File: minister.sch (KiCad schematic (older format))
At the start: 108 parts

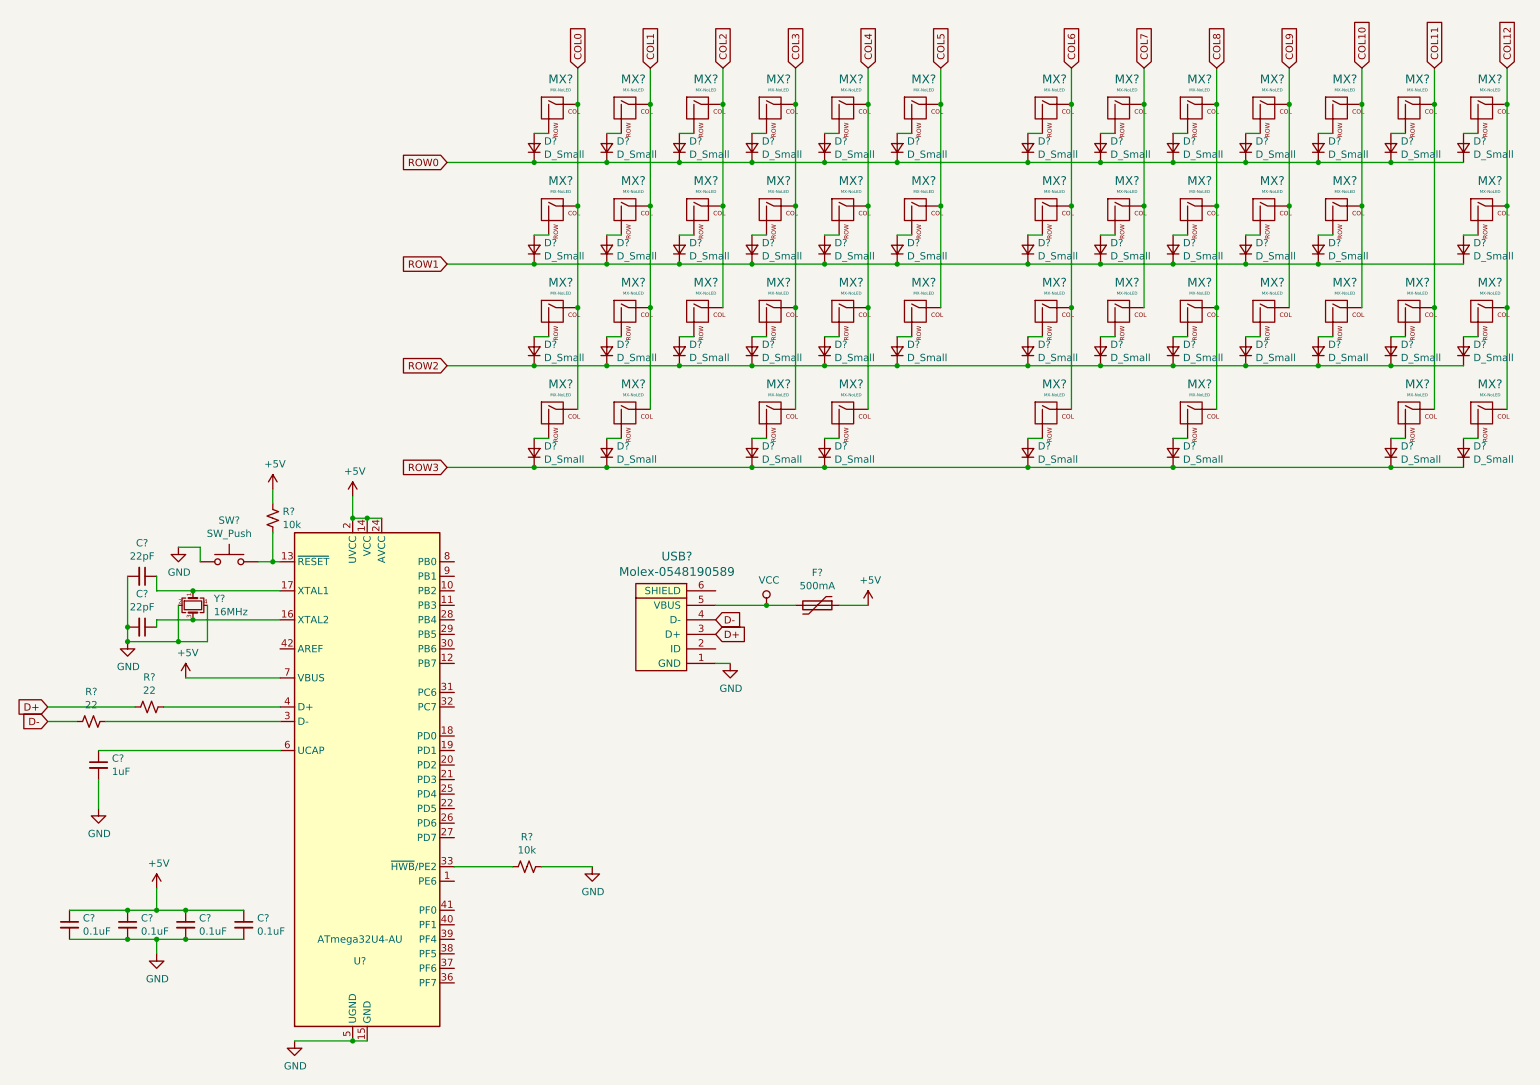
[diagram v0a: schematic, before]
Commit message: Assign Footprints
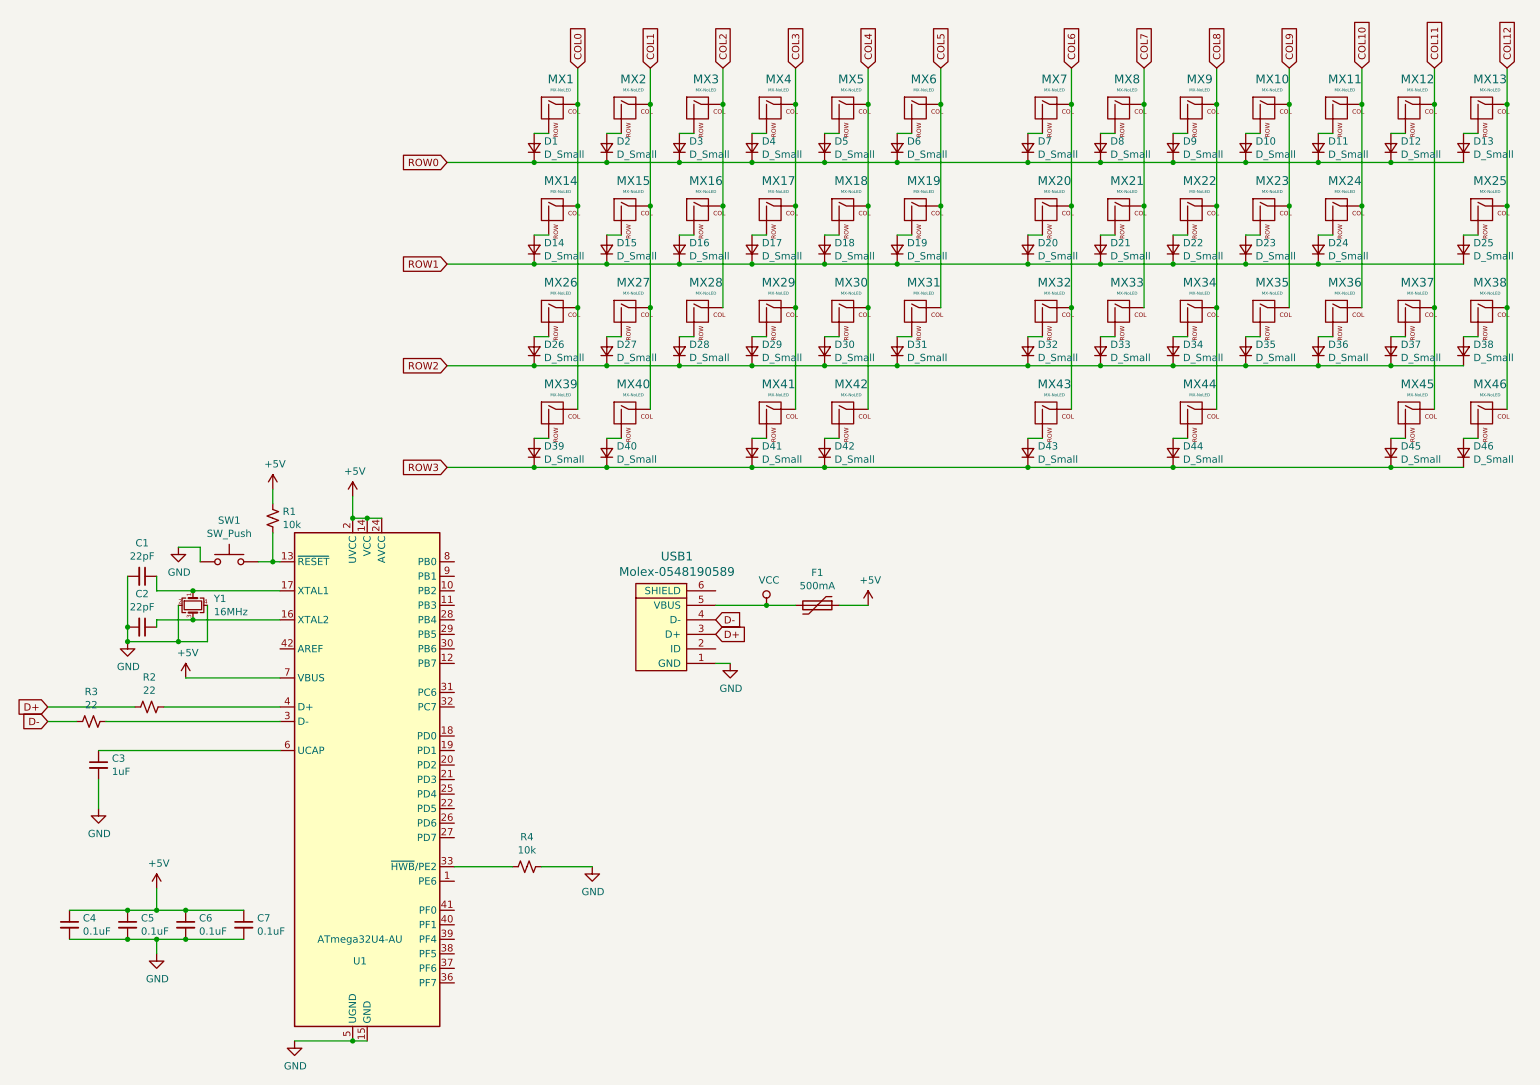
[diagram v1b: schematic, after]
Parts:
- C1, C2, C3, C4, C5, C6, C7: renamed from C?; footprint (none) -> Capacitor_SMD:C_0805_2012Metric
- D1, D10, D11, D12, D13, D14, D15, D16, D17, D18, D19, D2, D20, D21, D22, D23, D24, D25, D26, D27, D28, D29, D3, D30, D31, D32, D33, D34, D35, D36, D37, D38, D39, D4, D40, D41, D42, D43, D44, D45, D46, D5, D6, D7, D8, D9: renamed from D?; footprint (none) -> Diode_SMD:D_SOD-123
- F1: renamed from F?; footprint (none) -> Fuse:Fuse_1206_3216Metric
- MX1, MX10, MX11, MX12, MX13, MX14, MX15, MX16, MX17, MX18, MX19, MX2, MX20, MX21, MX22, MX23, MX24, MX25, MX26, MX27, MX28, MX29, MX3, MX30, MX31, MX32, MX33, MX34, MX35, MX36, MX37, MX38, MX39, MX4, MX40, MX41, MX42, MX43, MX44, MX45, MX46, MX5, MX6, MX7, MX8, MX9: renamed from MX?; footprint (none) -> MX_Only:MXOnly-1U
- R1, R2, R3, R4: renamed from R?; footprint (none) -> Resistor_SMD:R_0805_2012Metric
- SW1: renamed from SW?; footprint (none) -> random-keyboard-parts:SKQG-1155865
- USB1: renamed from USB?; footprint (none) -> random-keyboard-parts:Molex-0548190589
- Y1: renamed from Y?; footprint (none) -> Crystal:Crystal_SMD_3225-4Pin_3.2x2.5mm
- gave numbers to parts that had none: 1

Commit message: update footprints
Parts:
- MX1, MX10, MX11, MX12, MX13, MX15, MX16, MX17, MX18, MX19, MX2, MX20, MX21, MX22, MX23, MX24, MX27, MX28, MX29, MX3, MX30, MX31, MX32, MX33, MX34, MX35, MX36, MX37, MX4, MX5, MX6, MX7, MX8, MX9: footprint MX_Only:MXOnly-1U -> MX_Only:MXOnly-1U-Hotswap
- MX14, MX38, MX39, MX40, MX41, MX44, MX45, MX46: footprint MX_Only:MXOnly-1U -> MX_Only:MXOnly-1.25U-Hotswap
- MX25, MX26: footprint MX_Only:MXOnly-1U -> MX_Only:MXOnly-1.75U-Hotswap
- MX42: footprint MX_Only:MXOnly-1U -> MX_Only:MXOnly-2U-Hotswap
- MX43: footprint MX_Only:MXOnly-1U -> MX_Only:MXOnly-2.25U-Hotswap

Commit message: rearrange components
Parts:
- C7: value 0.1uF -> 10uF
- MX42: footprint MX_Only:MXOnly-2U-Hotswap -> MX_Only:MXOnly-2U-Hotswap-ReversedStabilizers
- MX43: footprint MX_Only:MXOnly-2.25U-Hotswap -> MX_Only:MXOnly-2.25U-Hotswap-ReversedStabilizers
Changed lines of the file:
@@
 P 2100 6650
 F 0 "C7" H 2192 6696 50  0000 L CNN
-F 1 "0.1uF" H 2192 6605 50  0000 L CNN
+F 1 "10uF" H 2192 6605 50  0000 L CNN
 F 2 "Capacitor_SMD:C_0805_2012Metric" H 2100 6650 50  0001 C CNN
 F 3 "~" H 2100 6650 50  0001 C CNN
@@
 F 0 "MX43" H 7683 3373 60  0000 C CNN
 F 1 "MX-NoLED" H 7683 3299 20  0000 C CNN
-F 2 "MX_Only:MXOnly-2.25U-Hotswap" H 7025 3125 60  0001 C CNN
+F 2 "MX_Only:MXOnly-2.25U-Hotswap-ReversedStabilizers" H 7025 3125 60  0001 C CNN
 F 3 "" H 7025 3125 60  0001 C CNN
 	1    7650 3150
@@
 F 0 "MX42" H 6283 3373 60  0000 C CNN
 F 1 "MX-NoLED" H 6283 3299 20  0000 C CNN
-F 2 "MX_Only:MXOnly-2U-Hotswap" H 5625 3125 60  0001 C CNN
+F 2 "MX_Only:MXOnly-2U-Hotswap-ReversedStabilizers" H 5625 3125 60  0001 C CNN
 F 3 "" H 5625 3125 60  0001 C CNN
 	1    6250 3150

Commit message: more routing
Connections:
- net COL0: now also U1.41 (PF0)
- net COL1: now also U1.40 (PF1)
- net COL10: now also U1.20 (PD2)
- net COL11: now also U1.19 (PD1)
- net COL12: now also U1.18 (PD0)
- net COL2: now also U1.39 (PF4)
- net COL3: now also U1.38 (PF5)
- net COL4: now also U1.37 (PF6)
- net COL5: now also U1.36 (PF7)
- net COL6: now also U1.26 (PD6)
- net COL7: now also U1.25 (PD4)
- net COL8: now also U1.22 (PD5)
- net COL9: now also U1.21 (PD3)
- net ROW0: now also U1.1 (PE6)
- net ROW1: now also U1.32 (PC7)
- net ROW2: now also U1.29 (PB5)
- net ROW3: now also U1.28 (PB4)
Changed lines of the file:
@@
 EESchema Schematic File Version 4
+LIBS:minister-cache
 EELAYER 30 0
 EELAYER END
@@
 Text GLabel 10800 750  1    50   Input ~ 0
 COL12
+Text GLabel 3550 6350 2    50   Input ~ 0
+ROW0
+Text GLabel 3550 5150 2    50   Input ~ 0
+ROW1
+Text GLabel 3550 4650 2    50   Input ~ 0
+ROW2
+Text GLabel 3550 4550 2    50   Input ~ 0
+ROW3
+Text GLabel 3550 6550 2    50   Input ~ 0
+COL0
+Text GLabel 3550 6650 2    50   Input ~ 0
+COL1
+Text GLabel 3550 6750 2    50   Input ~ 0
+COL2
+Text GLabel 3550 6850 2    50   Input ~ 0
+COL3
+Text GLabel 3550 6950 2    50   Input ~ 0
+COL4
+Text GLabel 3550 7050 2    50   Input ~ 0
+COL5
+Text GLabel 3550 5950 2    50   Input ~ 0
+COL6
+Text GLabel 3550 5750 2    50   Input ~ 0
+COL7
+Text GLabel 3550 5850 2    50   Input ~ 0
+COL8
+Text GLabel 3550 5650 2    50   Input ~ 0
+COL9
+Text GLabel 3550 5550 2    50   Input ~ 0
+COL10
+Text GLabel 3550 5450 2    50   Input ~ 0
+COL11
+Text GLabel 3550 5350 2    50   Input ~ 0
+COL12
 $EndSCHEMATC

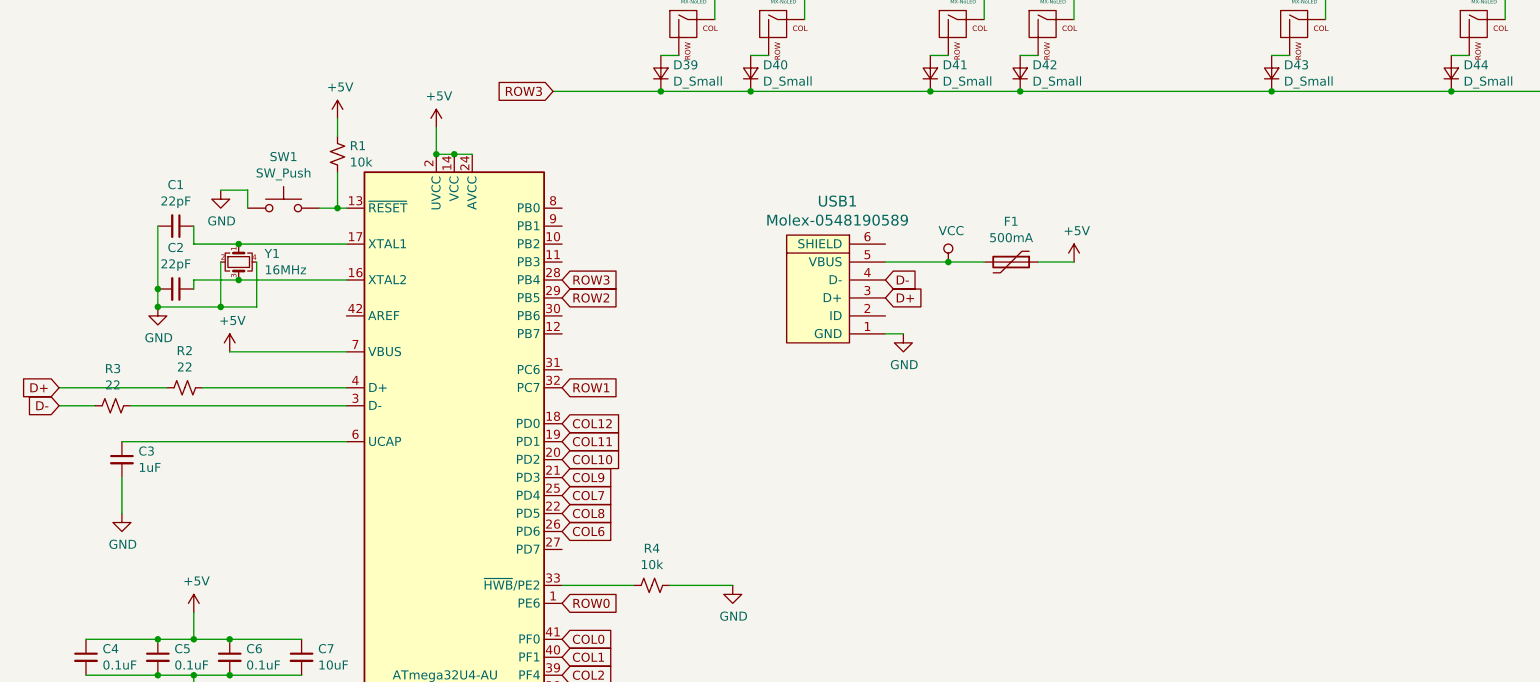
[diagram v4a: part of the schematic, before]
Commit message: replace usb and generate output files
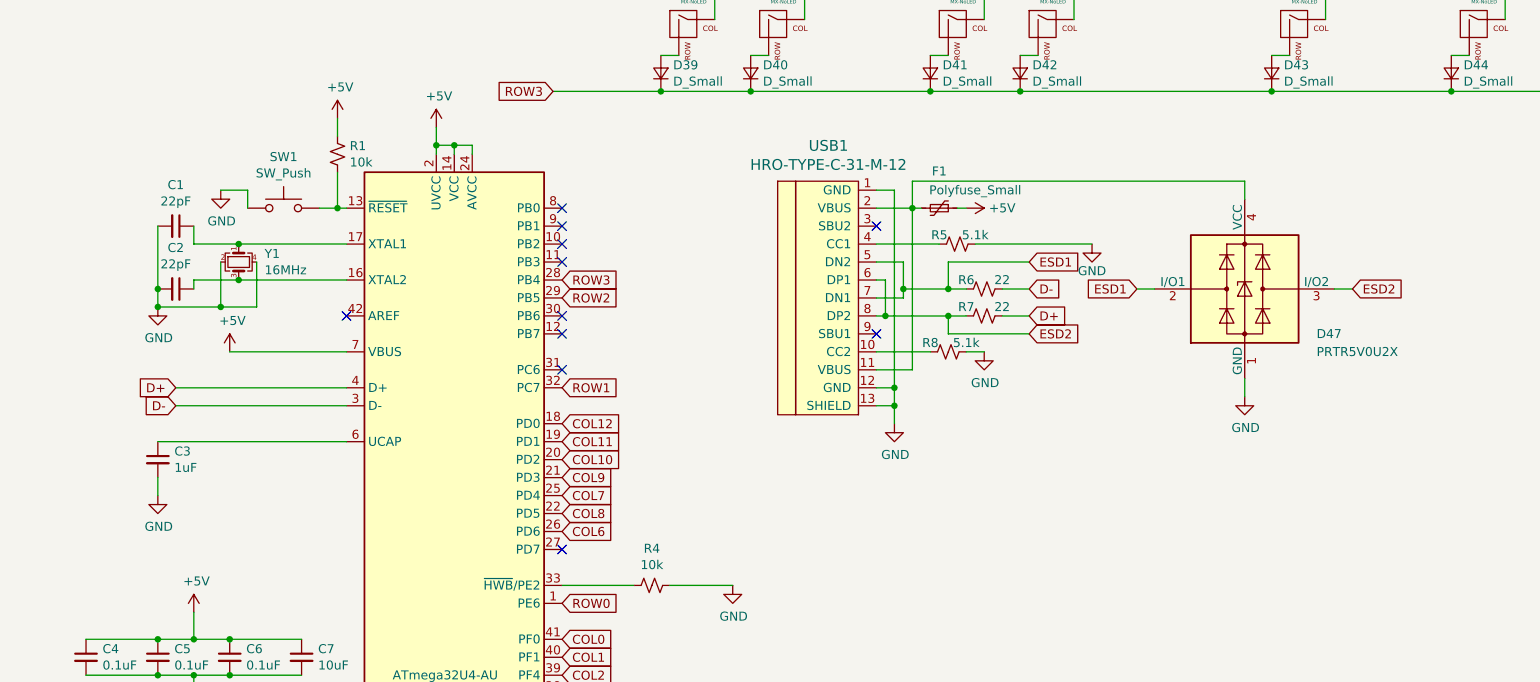
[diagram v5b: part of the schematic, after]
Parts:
- removed F1: 500mA, Fuse:Fuse_1206_3216Metric, symbol Device:Polyfuse
- removed R2, R3: 22, Resistor_SMD:R_0805_2012Metric, symbol Device:R_Small_US
- removed USB1: Molex-0548190589, random-keyboard-parts:Molex-0548190589, symbol random-keyboard-parts:Molex-0548190589
- added D47: PRTR5V0U2X, Package_TO_SOT_SMD:SOT-143_Handsoldering, symbol Power_Protection:PRTR5V0U2X
- added F1: Polyfuse_Small, Fuse:Fuse_1206_3216Metric, symbol Device:Polyfuse_Small
- added R5, R8: 5.1k, Resistor_SMD:R_0805_2012Metric, symbol Device:R_Small_US
- added R6, R7: 22, Resistor_SMD:R_0805_2012Metric, symbol Device:R_Small_US
- added USB1: HRO-TYPE-C-31-M-12, Connector_USB:USB_C_Receptacle_HRO_TYPE-C-31-M-12, symbol Type-C:HRO-TYPE-C-31-M-12
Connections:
- net +5V: now also F1.1
- net D+: now also U1.4 (D+), R7.1
- net D-: now also U1.3 (D-), R6.1
- net GND: now also D47.1 (GND), R5.1, R8.1, USB1.1 (GND), USB1.12 (GND), USB1.13 (SHIELD)
- new net: R8.2, USB1.10 (CC2)
- new net: D47.4 (VCC), F1.2, USB1.11 (VBUS), USB1.2 (VBUS)
- new net: R5.2, USB1.4 (CC1)
- new net ESD1: D47.2 (I/O1), R6.2, USB1.5 (DN2), USB1.7 (DN1)
- new net ESD2: D47.3 (I/O2), R7.2, USB1.6 (DP1), USB1.8 (DP2)
- no-connect marks 0 -> 11
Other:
- moved on the sheet: C3

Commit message: not sure
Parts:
- USB1: footprint Connector_USB:USB_C_Receptacle_HRO_TYPE-C-31-M-12 -> Type-C:HRO-TYPE-C-31-M-12-HandSoldering
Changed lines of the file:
@@
 U 1 1 5E9D7171
 P 5200 4600
-F 0 "USB1" H 5033 5397 60  0000 C CNN
-F 1 "HRO-TYPE-C-31-M-12" H 5033 5291 60  0000 C CNN
-F 2 "Connector_USB:USB_C_Receptacle_HRO_TYPE-C-31-M-12" H 5200 4600 60  0001 C CNN
+F 0 "USB1" H 4850 5250 60  0000 C CNN
+F 1 "HRO-TYPE-C-31-M-12" H 5300 5350 60  0000 C CNN
+F 2 "Type-C:HRO-TYPE-C-31-M-12-HandSoldering" H 5200 4600 60  0001 C CNN
 F 3 "" H 5200 4600 60  0001 C CNN
 	1    5200 4600

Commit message: add isp
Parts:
- added J1: AVR-ISP-6, Connector_IDC:IDC-Header_2x03_P2.54mm_Vertical, symbol Connector:AVR-ISP-6
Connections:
- net +5V: now also J1.2 (VCC)
- net GND: now also J1.6 (GND)
- net MOSI: now reaches U1.10 (PB2)
- net MOSI: now also J1.4 (MOSI)
- net MISO: now reaches U1.11 (PB3)
- net MISO: now also J1.1 (MISO)
- net RST: now reaches R1.2, SW1.2, U1.13 (~RESET)
- net RST: now also J1.5 (~RST)
- net SCK: now reaches U1.9 (PB1)
- net SCK: now also J1.3 (SCK)
- no-connect marks 11 -> 8
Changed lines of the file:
@@
 Wire Wire Line
 	5500 4000 5500 4150
-Wire Wire Line
-	7950 4600 7850 4600
-Text GLabel 7950 4600 2    50   Input ~ 0
+Text GLabel 7850 4600 2    50   Input ~ 0
 ESD2
-Text GLabel 6750 4600 0    50   Input ~ 0
+Text GLabel 6850 4600 0    50   Input ~ 0
 ESD1
-Wire Wire Line
-	6750 4600 6850 4600
 $Comp
 L power:GND #PWR0115
@@
 NoConn ~ 3550 4850
 NoConn ~ 3550 4750
-NoConn ~ 3550 4450
-NoConn ~ 3550 4350
-NoConn ~ 3550 4250
 NoConn ~ 3550 4150
 NoConn ~ 3550 5050
@@
 	1    0    0    -1
 $EndComp
+$Comp
+L Connector:AVR-ISP-6 J1
+U 1 1 5EAF29DC
+P 5750 6300
+F 0 "J1" H 5471 6396 50  0000 R CNN
+F 1 "AVR-ISP-6" H 5471 6305 50  0000 R CNN
+F 2 "Connector_IDC:IDC-Header_2x03_P2.54mm_Vertical" V 5500 6350 50  0001 C CNN
+F 3 " ~" H 4475 5750 50  0001 C CNN
+	1    5750 6300
+	1    0    0    -1
+$EndComp
+Text GLabel 6150 6200 2    50   Input ~ 0
+MOSI
+Text GLabel 6150 6100 2    50   Input ~ 0
+MISO
+Text GLabel 6150 6300 2    50   Input ~ 0
+SCK
+Text GLabel 6150 6400 2    50   Input ~ 0
+RST
+$Comp
+L power:+5V #PWR0116
+U 1 1 5EB30166
+P 5650 5700
+F 0 "#PWR0116" H 5650 5550 50  0001 C CNN
+F 1 "+5V" H 5665 5873 50  0000 C CNN
+F 2 "" H 5650 5700 50  0001 C CNN
+F 3 "" H 5650 5700 50  0001 C CNN
+	1    5650 5700
+	1    0    0    -1
+$EndComp
+$Comp
+L power:GND #PWR0117
+U 1 1 5EB30E0E
+P 5650 6800
+F 0 "#PWR0117" H 5650 6550 50  0001 C CNN
+F 1 "GND" H 5655 6627 50  0000 C CNN
+F 2 "" H 5650 6800 50  0001 C CNN
+F 3 "" H 5650 6800 50  0001 C CNN
+	1    5650 6800
+	1    0    0    -1
+$EndComp
+Wire Wire Line
+	5650 6700 5650 6800
+Wire Wire Line
+	5650 5800 5650 5700
+Text GLabel 3550 4450 2    50   Input ~ 0
+MISO
+Text GLabel 3550 4350 2    50   Input ~ 0
+MOSI
+Text GLabel 3550 4250 2    50   Input ~ 0
+SCK
+Text GLabel 2250 4250 0    50   Input ~ 0
+RST
+Wire Wire Line
+	2250 4250 2300 4250
+Wire Wire Line
+	2300 4250 2300 4150
 $EndSCHEMATC

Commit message: clean up and touch up pcb
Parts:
- C1, C2: Field4 (none) -> C1804
- C3: Field4 (none) -> C28323
- C4, C5, C6: Field4 (none) -> C49678
- C7: Field4 (none) -> C307523
- D1, D10, D11, D12, D13, D14, D15, D16, D17, D18, D19, D2, D20, D21, D22, D23, D24, D25, D26, D27, D28, D29, D3, D30, D31, D32, D33, D34, D35, D36, D37, D38, D39, D4, D40, D41, D42, D43, D44, D45, D46, D5, D6, D7, D8, D9: Field4 (none) -> C81598
- D47: Field4 (none) -> C78442
- F1: Field4 (none) -> C151162
- R1, R4: Field4 (none) -> C17414
- R5, R8: Field4 (none) -> C27834
- R6, R7: Field4 (none) -> C17561
- SW1: Field4 (none) -> C318884
- Y1: Field4 (none) -> C89379
